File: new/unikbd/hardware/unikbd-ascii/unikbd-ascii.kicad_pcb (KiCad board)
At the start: 2 copper layers, 88.9 x 119.4 mm, 17 parts, among them J1 Reset/Clr, J2 Apple 1, J3 Apple 2, J4 Keyboard, J5 ISP header, J6 UART, U1 ATmega328P, U2 74LS154, U3 74LS166

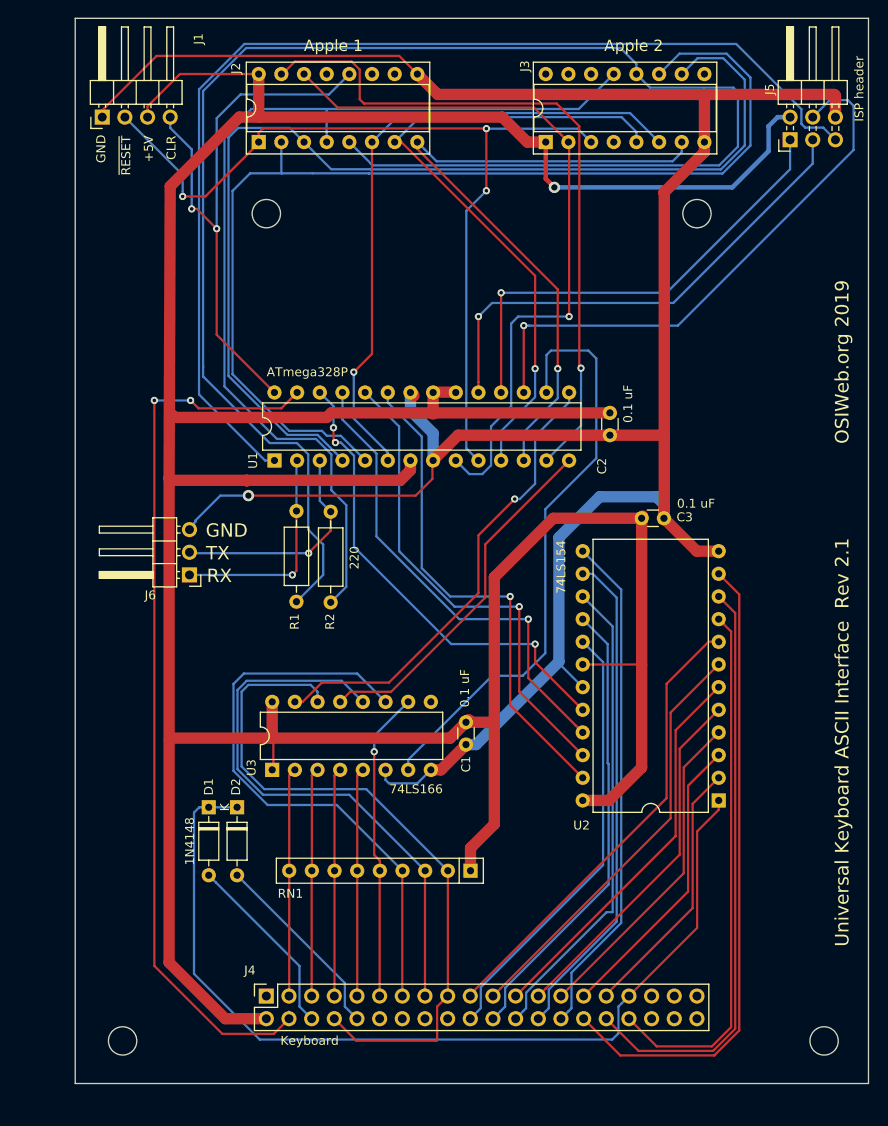
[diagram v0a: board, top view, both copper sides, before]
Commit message: * added DIP switches for controlling options (and diodes, since they are part of   the matrix.
* replaced 74154 with a pair of more readily available 74LS138's

* fixed off-by-one error on keyboard connector.

* added serial I/O, for bootloader, serial output option, debugging.
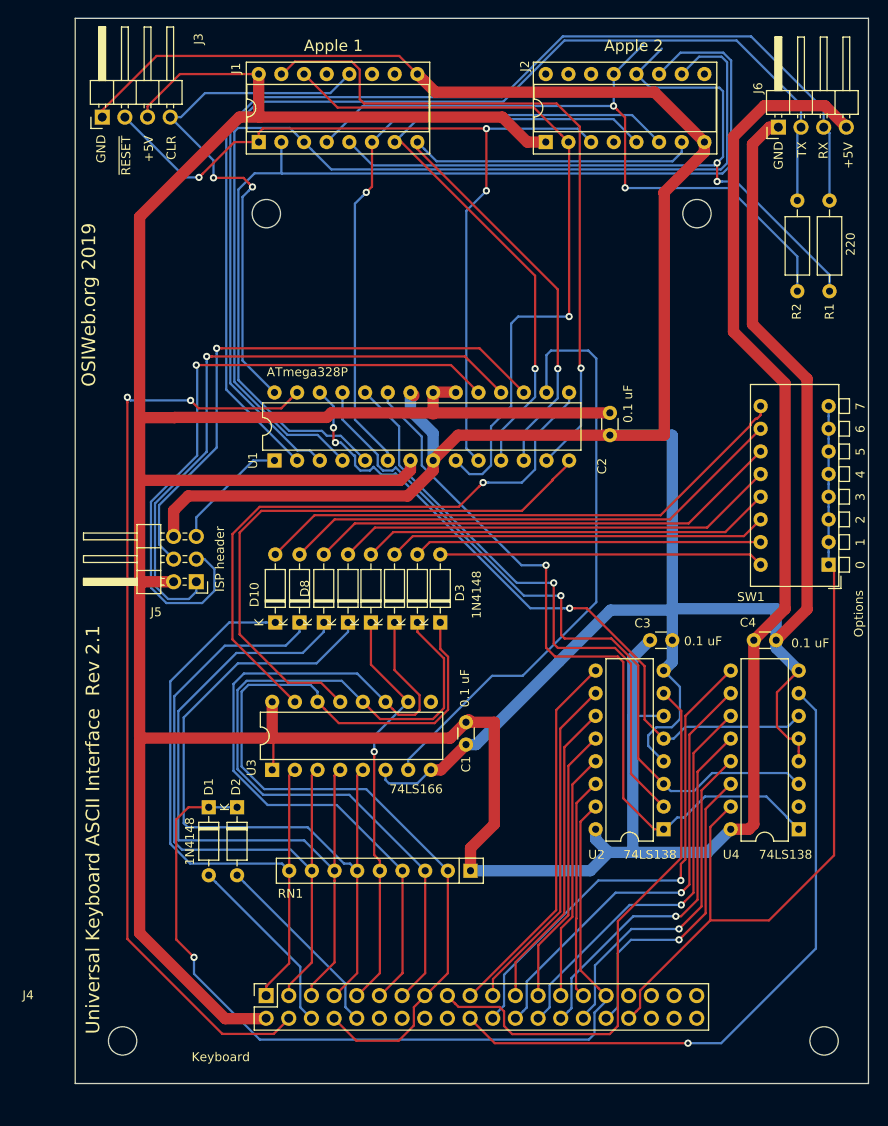
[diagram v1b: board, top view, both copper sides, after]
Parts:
- removed the J1 at (166.9, 74.6)
- added C4: 0.1 uF, Capacitor_THT:C_Disc_D3.0mm_W1.6mm_P2.50mm, F.Cu at (239.9, 133.2)
- added D10: 1N4148, Diode_THT:D_DO-35_SOD27_P7.62mm_Horizontal, F.Cu at (186.3, 131.2)
- added D3: 1N4148, Diode_THT:D_DO-35_SOD27_P7.62mm_Horizontal, F.Cu at (204.7, 131.2)
- added D4: 1N4148, Diode_THT:D_DO-35_SOD27_P7.62mm_Horizontal, F.Cu at (202.2, 131.2)
- added D5: 1N4148, Diode_THT:D_DO-35_SOD27_P7.62mm_Horizontal, F.Cu at (199.6, 131.2)
- added D6: 1N4148, Diode_THT:D_DO-35_SOD27_P7.62mm_Horizontal, F.Cu at (197.0, 131.2)
- added D7: 1N4148, Diode_THT:D_DO-35_SOD27_P7.62mm_Horizontal, F.Cu at (194.4, 131.2)
- added D8: 1N4148, Diode_THT:D_DO-35_SOD27_P7.62mm_Horizontal, F.Cu at (191.7, 131.2)
- added D9: 1N4148, Diode_THT:D_DO-35_SOD27_P7.62mm_Horizontal, F.Cu at (189.0, 131.2)
- added J3: Reset/Clr, Connector_PinHeader_2.54mm:PinHeader_1x04_P2.54mm_Horizontal, F.Cu at (166.9, 74.6)
- added SW1: Options, Button_Switch_THT:SW_DIP_SPSTx08_Piano_CTS_Series194-8MSTN_W7.62mm_P2.54mm, F.Cu at (248.3, 124.7)
- added U4: 74LS138, Package_DIP:DIP-16_W7.62mm, F.Cu at (244.9, 154.4)
- J4: footprint Connector_PinSocket_2.54mm:PinSocket_2x20_P2.54mm_Vertical -> unikbd:PinHeader_2x20_P2.54mm_Vertical
- J6: footprint Connector_PinHeader_2.54mm:PinHeader_1x03_P2.54mm_Horizontal -> Connector_PinHeader_2.54mm:PinHeader_1x04_P2.54mm_Horizontal
- U2: value 74LS154 -> 74LS138; footprint Package_DIP:DIP-24_W15.24mm -> Package_DIP:DIP-16_W7.62mm
- moved J5 83.0 mm to (177.4, 126.6), turned to 180 degrees
- moved J6 82.9 mm to (242.6, 75.7), turned to 90 degrees
- moved R1 69.1 mm to (248.4, 94.1)
- moved R2 62.9 mm to (244.8, 94.1)
- moved C3 13.7 mm to (228.2, 133.2)
- moved U2 6.96 mm to (229.8, 154.4)
- moved J4 2.52 mm to (185.4, 175.6)
- renumbered J2 to J1, J3 to J2
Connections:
- J4 pad 1: Net-(J4-Pad1) -> /Col7
- J4 pad 11: /Col3 -> /Col2
- J4 pad 13: /Col2 -> /Col1
- J4 pad 15: /Col1 -> /Col0
- J4 pad 17: /Col0 -> /Row7
- J4 pad 19: /Row7 -> /Row6
- J4 pad 21: /Row6 -> /Row5
- J4 pad 23: /Row5 -> /Row4
- J4 pad 25: /Row4 -> /Row3
- J4 pad 27: /Row3 -> /Row2
- J4 pad 29: /Row2 -> /Row1
- J4 pad 3: /Col7 -> /Col6
- J4 pad 31: /Row1 -> /Row0
- J4 pad 33: /Row0 -> Net-(J4-Pad33)
- J4 pad 5: /Col6 -> /Col5
- J4 pad 7: /Col5 -> /Col4
- J4 pad 9: /Col4 -> /Col3
- J6 pad 1: /Rx -> GND
- J6 pad 3: GND -> /Rx
- U2 pad 1: /Row0 -> Net-(U1-Pad23)
- U2 pad 10: /Row9 -> /Row5
- U2 pad 11: /Row10 -> /Row4
- U2 pad 12: GND -> /Row3
- U2 pad 13: /Row11 -> /Row2
- U2 pad 14: /Row12 -> /Row1
- U2 pad 15: /Row13 -> /Row0
- U2 pad 16: /Row14 -> +5V
- U2 pad 2: /Row1 -> Net-(U1-Pad24)
- U2 pad 3: /Row2 -> Net-(U1-Pad25)
- U2 pad 4: /Row3 -> GND
- U2 pad 5: /Row4 -> Net-(U1-Pad26)
- U2 pad 6: /Row5 -> +5V
- U2 pad 7: /Row6 -> /Row7
- U2 pad 8: /Row7 -> GND
- U2 pad 9: /Row8 -> /Row6
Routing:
- net /~RESET: track 124.6 -> 13.5 mm
- net /Rx: track 24.7 -> 125.9 mm, vias 1 -> 0
- net /Tx: track 25.3 -> 124.0 mm, vias 1 -> 0
- net /D0: track 182.3 -> 86.1 mm, vias 0 -> 2
- net GND: track 274.7 -> 366.1 mm, vias 1 -> 0
- net +5V: track 430.4 -> 492.8 mm, vias 1 -> 0
- net Net-(D10-Pad2): track 0.00 -> 62.0 mm
- net /Col4: track 25.7 -> 84.0 mm
- net Net-(D9-Pad2): track 0.00 -> 57.5 mm
- net /Col5: track 26.0 -> 81.1 mm
- net Net-(D8-Pad2): track 0.00 -> 53.7 mm
- net /Col6: track 25.6 -> 77.9 mm
- net Net-(D7-Pad2): track 0.00 -> 50.0 mm
- net /Col7: track 25.5 -> 74.0 mm
- net Net-(D6-Pad2): track 0.00 -> 46.4 mm
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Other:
- board text added: "0"
- board text added: "1"
- board text added: "2"
- board text added: "3"
- board text added: "4"
- board text added: "5"
- board text added: "6"
- board text added: "7"
